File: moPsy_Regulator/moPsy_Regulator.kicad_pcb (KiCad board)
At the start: 2 copper layers, 96.5 x 50.8 mm, 23 parts, among them J1 Conn_01x01_Pin, J2 Conn_01x01_Pin, J3 Conn_01x01_Pin, J4 Conn_01x01_Pin, Q1 BD201, Q2 BC337, U1 LM723_DIP14

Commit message: Small fixes and Greographic Renumeration
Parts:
- renumbered C4 to C1, C1 to C4, J4 to J3, J3 to J4
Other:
- board text removed: "0R"
- board text removed: "DNP"
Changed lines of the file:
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@@
 		(descr "C, Disc series, Radial, pin pitch=5.00mm, , diameter*width=4.3*1.9mm^2, Capacitor, http://www.vishay.com/docs/45233/krseries.pdf")
 		(tags "C Disc series Radial pin pitch 5.00mm  diameter 4.3mm width 1.9mm Capacitor")
-		(property "Reference" "C4"
+		(property "Reference" "C1"
 			(at 2.54 -0.204999 360)
 			(layer "F.SilkS")
@@
 		(layer "F.Cu")
 		(at 191.77 96.52)
-		(property "Reference" "J3"
+		(property "Reference" "J4"
 			(at 7 0 360)
 			(layer "F.SilkS")
@@
 		(layer "F.Cu")
 		(at 177.84 96.52)
-		(property "Reference" "J4"
+		(property "Reference" "J3"
 			(at 7 0 360)
 			(layer "F.SilkS")
@@
 		(descr "CP, Radial series, Radial, pin pitch=7.50mm, , diameter=16mm, Electrolytic Capacitor")
 		(tags "CP Radial series Radial pin pitch 7.50mm  diameter 16mm Electrolytic Capacitor")
-		(property "Reference" "C1"
+		(property "Reference" "C4"
 			(at 1.27 -3.81 180)
 			(layer "F.SilkS")
@@
 		)
 	)
+	(gr_circle
+		(center 136.144 91.567)
+		(end 136.271 91.567)
+		(stroke
+			(width 0.1)
+			(type solid)
+		)
+		(fill solid)
+		(layer "F.SilkS")
+	)
+	(gr_line
+		(start 145.161 90.297)
+		(end 147.701 90.297)
+		(stroke
+			(width 0.1)
+			(type default)
+		)
+		(layer "F.SilkS")
+	)
+	(gr_circle
+		(center 145.161 90.297)
+		(end 145.288 90.297)
+		(stroke
+			(width 0.1)
+			(type solid)
+		)
+		(fill solid)
+		(layer "F.SilkS")
+	)
+	(gr_circle
+		(center 147.701 90.297)
+		(end 147.828 90.297)
+		(stroke
+			(width 0.1)
+			(type solid)
+		)
+		(fill solid)
+		(layer "F.SilkS")
+	)
 	(gr_line
 		(start 132.715 89.408)
@@
 	)
 	(gr_line
+		(start 133.604 91.567)
+		(end 136.144 91.567)
+		(stroke
+			(width 0.1)
+			(type default)
+		)
+		(layer "F.SilkS")
+	)
+	(gr_circle
+		(center 133.604 91.567)
+		(end 133.731 91.567)
+		(stroke
+			(width 0.1)
+			(type solid)
+		)
+		(fill solid)
+		(layer "F.SilkS")
+	)
+	(gr_line
 		(start 132.715 89.408)
 		(end 131.191 87.884)
@@
 	)
 	(gr_line
+		(start 138.938 91.821)
+		(end 139.446 91.186)
+		(stroke
+			(width 0.1)
+			(type default)
+		)
+		(layer "F.SilkS")
+	)
+	(gr_line
 		(start 132.715 91.948)
 		(end 132.715 89.408)
@@
 	)
 	(gr_line
+		(start 138.938 91.186)
+		(end 139.446 91.821)
+		(stroke
+			(width 0.1)
+			(type default)
+		)
+		(layer "F.SilkS")
+	)
+	(gr_line
+		(start 150.368 89.9795)
+		(end 150.876 90.6145)
+		(stroke
+			(width 0.1)
+			(type default)
+		)
+		(layer "F.SilkS")
+	)
+	(gr_line
 		(start 114.7445 94.742)
 		(end 113.0935 88.265)
@@
 		(layer "F.SilkS")
 	)
+	(gr_line
+		(start 150.368 90.6145)
+		(end 150.876 89.9795)
+		(stroke
+			(width 0.1)
+			(type default)
+		)
+		(layer "F.SilkS")
+	)
 	(gr_rect
 		(start 101.6 50.8)
@@
 		)
 	)
-	(gr_text "0R"
-		(at 136.525 92.075 0)
-		(layer "F.SilkS")
-		(effects
-			(font
-				(size 0.8 0.8)
-				(thickness 0.1)
-			)
-			(justify right bottom)
-		)
-	)
 	(gr_text "500R"
 		(at 136.525 90.805 0)
@@
 		)
 	)
-	(gr_text "DNP"
-		(at 140.335 92.075 0)
-		(layer "F.SilkS")
-		(effects
-			(font
-				(size 0.8 0.8)
-				(thickness 0.1)
-			)
-			(justify right bottom)
-		)
-	)
 	(gr_text "V_{OUT}"
 		(at 191.77 100.838 0)
@@
 		)
 	)
-	(gr_text "DNP"
-		(at 151.765 90.805 0)
-		(layer "F.SilkS")
-		(effects
-			(font
-				(size 0.8 0.8)
-				(thickness 0.1)
-			)
-			(justify right bottom)
-		)
-	)
 	(gr_text "1k"
 		(at 147.955 92.075 0)
@@
 		)
 	)
-	(gr_text "0R"
-		(at 147.955 90.805 0)
-		(layer "F.SilkS")
-		(effects
-			(font
-				(size 0.8 0.8)
-				(thickness 0.1)
-			)
-			(justify right bottom)
-		)
-	)
 	(segment
 		(start 141.605 68.58)
@@
 		)
 	)
+	(group ""
+		(members "07f13dc1-afab-4ed4-8025-a04d3f19f5e8" "46d33b63-7861-44c6-9e5e-61609bf35534"
+			"4a4c9e23-7bda-48f4-84c6-1a3d4b97ff38"
+		)
+	)
+	(group ""
+		(members "099868f8-a03c-43de-a861-8a08c08919b7" "15b0ae34-e2e2-4f86-aa7e-9aa4b8101d5a"
+			"16f80a3a-df75-4565-bd00-cf7e78347348"
+		)
+	)
+	(group ""
+		(members "94caba43-0bac-4706-8947-572840e6577d" "d404e082-68a9-48c7-a333-d59657457921")
+	)
+	(group ""
+		(members "de9c32ee-4f5a-437d-88a5-43bda4c5d7c3" "e727caf5-7b4a-46a1-b502-8a09c3ae42dc")
+	)
 )

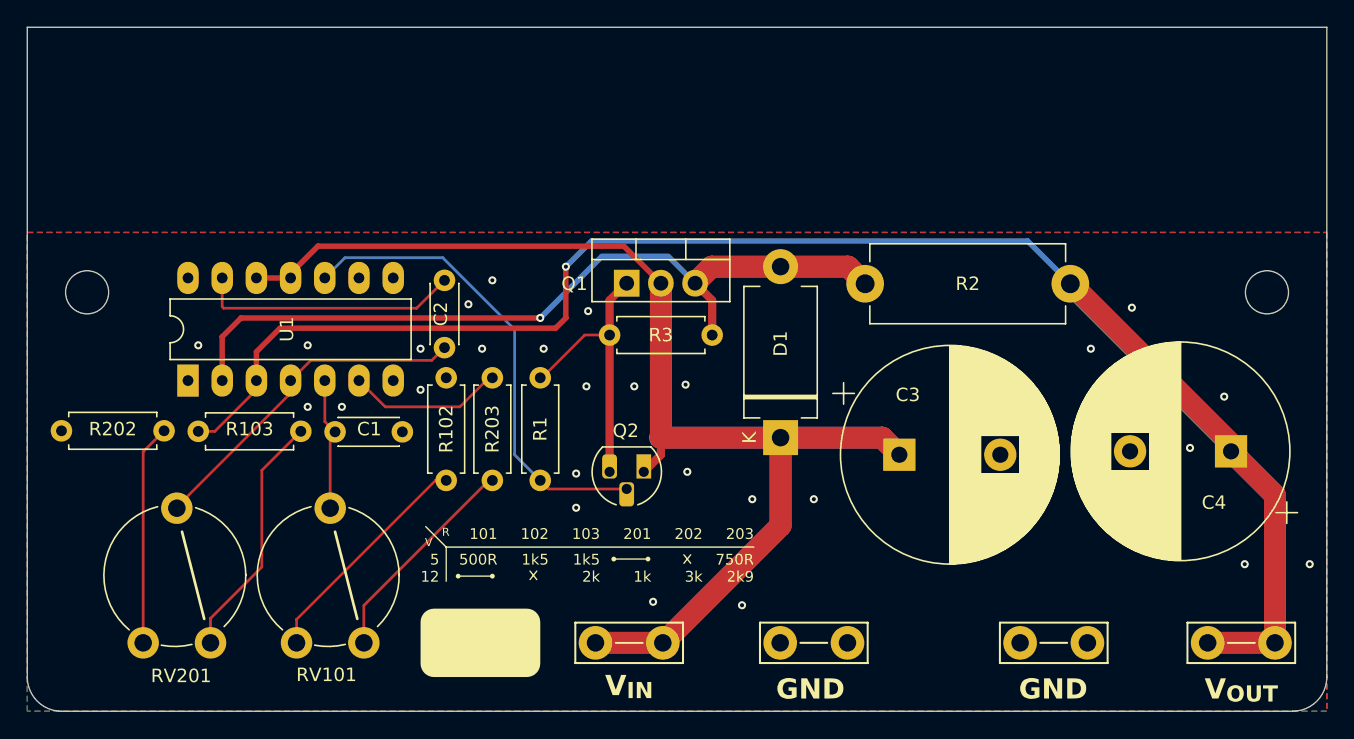
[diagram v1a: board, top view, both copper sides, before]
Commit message: Improve the voltage selection and layout
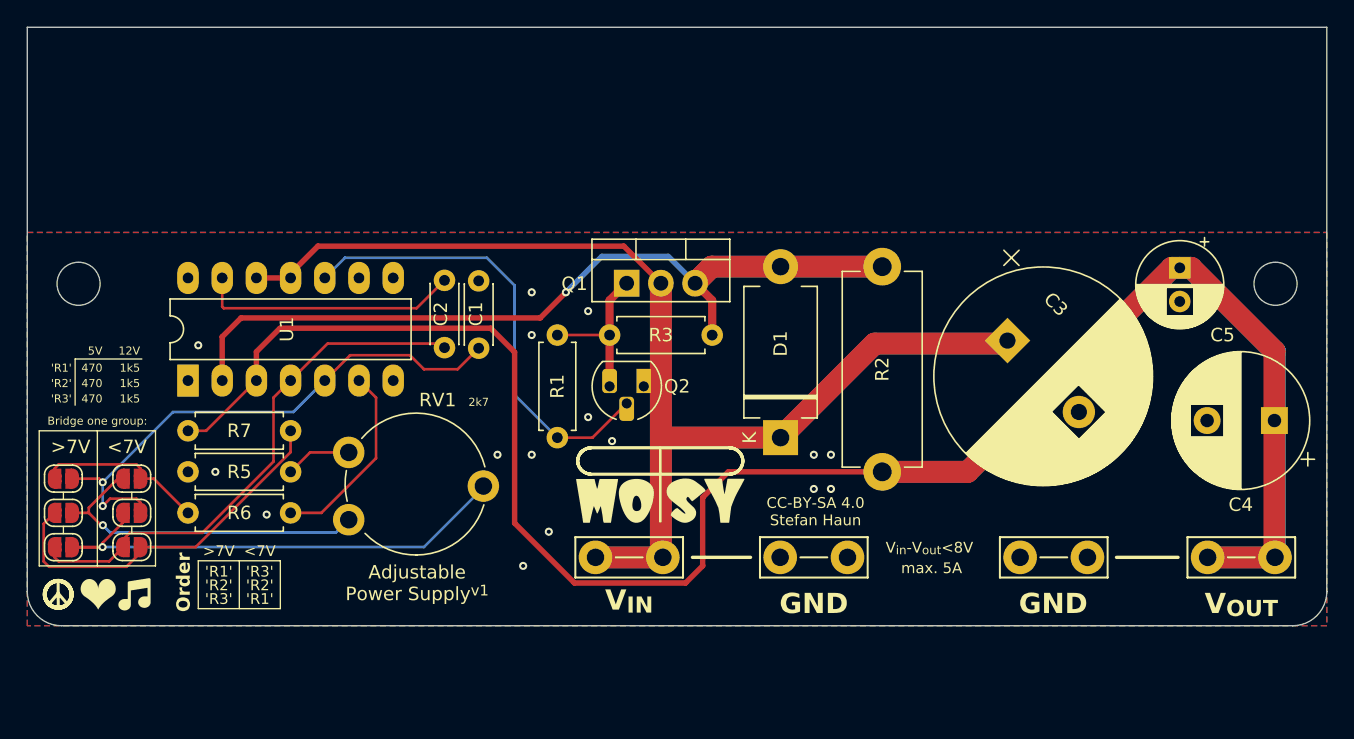
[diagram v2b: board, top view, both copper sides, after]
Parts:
- removed R102, R202: "R2", Resistor_THT:R_Axial_DIN0207_L6.3mm_D2.5mm_P7.62mm_Horizontal
- removed R103, R203: "R3", Resistor_THT:R_Axial_DIN0207_L6.3mm_D2.5mm_P7.62mm_Horizontal
- removed REF** (x2): MountingHole_3.2mm_M3, MountingHole:MountingHole_3.2mm_M3
- removed RV101, RV201: "R1", Potentiometer_THT:Potentiometer_Piher_PT-10-V10_Vertical
- added C5: 22u, Capacitor_THT:CP_Radial_D6.3mm_P2.50mm, F.Cu at (187.2, 68.7)
- added JP11: SolderJumper_2_Open, Jumper:SolderJumper-2_P1.3mm_Open_RoundedPad1.0x1.5mm, F.Cu at (109.4, 84.3)
- added JP12: SolderJumper_2_Open, Jumper:SolderJumper-2_P1.3mm_Open_RoundedPad1.0x1.5mm, F.Cu at (109.4, 86.9)
- added JP13: SolderJumper_2_Open, Jumper:SolderJumper-2_P1.3mm_Open_RoundedPad1.0x1.5mm, F.Cu at (109.4, 89.4)
- added JP21: SolderJumper_2_Open, Jumper:SolderJumper-2_P1.3mm_Open_RoundedPad1.0x1.5mm, F.Cu at (104.3, 86.9)
- added JP22: SolderJumper_2_Open, Jumper:SolderJumper-2_P1.3mm_Open_RoundedPad1.0x1.5mm, F.Cu at (104.3, 89.4)
- added JP23: SolderJumper_2_Open, Jumper:SolderJumper-2_P1.3mm_Open_RoundedPad1.0x1.5mm, F.Cu at (104.3, 84.3)
- added R5: "R2", Resistor_THT:R_Axial_DIN0207_L6.3mm_D2.5mm_P7.62mm_Horizontal, F.Cu at (121.2, 83.8)
- added R6: "R1"/"R3", Resistor_THT:R_Axial_DIN0207_L6.3mm_D2.5mm_P7.62mm_Horizontal, F.Cu at (121.2, 86.9)
- added R7: "R1"/"R3", Resistor_THT:R_Axial_DIN0207_L6.3mm_D2.5mm_P7.62mm_Horizontal, F.Cu at (113.5, 80.8)
- added REF1: MountingHole_3.2mm_M3, MountingHole:MountingHole_3.2mm_M3, F.Cu at (194.3, 69.8)
- added REF2: MountingHole_3.2mm_M3, MountingHole:MountingHole_3.2mm_M3, F.Cu at (105.4, 69.8)
- added RV1: "P1", Potentiometer_THT:Potentiometer_Piher_PT-10-V10_Vertical, F.Cu at (125.5, 87.4)
- C4: value 2200u -> 220u; footprint Capacitor_THT:CP_Radial_D16.0mm_P7.50mm -> Capacitor_THT:CP_Radial_D10.0mm_P5.00mm
- moved C1 12.3 mm to (135.1, 74.6), turned to 90 degrees
- moved C3 11.7 mm to (174.4, 74.1), turned to -45 degrees
- moved J1 6.35 mm to (146.3, 90.2)
- moved J2 6.35 mm to (160.0, 90.2)
- moved J3 6.35 mm to (177.8, 90.2)
- moved J4 6.35 mm to (191.8, 90.2)
- moved Q2 6.35 mm to (147.4, 77.5)
- moved C4 3.95 mm to (194.2, 80.0)
- moved R1 3.42 mm to (141.0, 81.3)
- moved R2 1.80 mm to (165.1, 68.6), turned to -90 degrees
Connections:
- net Net-(U1-+) renamed LV_{center}
- net Net-(U1--) renamed HV_{center}
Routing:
- net V_{out}: track 151.8 -> 194.9 mm, vias 1 -> 0
- net Net-(JP12-B): track 0.00 -> 37.9 mm, vias 0 -> 1
- net LV_{center}: track 9.94 -> 41.0 mm, vias 0 -> 2
- net HV_{top}: track 0.00 -> 28.5 mm
- net Net-(JP11-B): track 0.00 -> 25.4 mm, vias 0 -> 1
- net Net-(R103-Pad2): track 18.5 -> 0.00 mm
- net Net-(R102-Pad1): track 17.1 -> 0.00 mm
- net Net-(R202-Pad1): track 16.4 -> 0.00 mm
- net Net-(R203-Pad2): track 16.2 -> 0.00 mm
- net HV_{center}: track 25.4 -> 40.7 mm
- net LV_{top}: track 0.00 -> 13.3 mm
- net Net-(Q1-B): track 21.0 -> 12.1 mm
- net Net-(R5-Pad1): track 0.00 -> 4.92 mm
- net Net-(U1-VREF): track 11.6 -> 14.3 mm
- net Net-(D1-A): track 73.4 -> 74.9 mm
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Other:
- board size 96.5 x 50.8 mm -> 96.5 x 44.5 mm
- board text added: "'R1'"
- board text added: "'R2'"
- board text added: "'R3'"
- board text added: "12V"
- board text added: "2k7"
- board text added: "470"
- board text added: "5V"
- board text added: "<7V"
- board text added: ">7V"
- board text added: "Adjustable Power Supply^{v1}"
- board text added: "Bridge one group:"
- board text added: "CC-BY-SA 4.0 Stefan Haun"
- board text added: "Order"
- board text added: "V_{in}-V_{out}<8V"
- board text added: "max. 5A"
- board text removed: "101"
- board text removed: "102"
- board text removed: "103"
- board text removed: "12"
- board text removed: "1k"
- board text removed: "201"
- board text removed: "202"
- board text removed: "203"
- board text removed: "2k"
- board text removed: "2k9"
- board text removed: "3k"
- board text removed: "5"
- board text removed: "500R"
- board text removed: "750R"
- board text removed: "R"
- board text removed: "V"

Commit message: Geographical Reannotation and some minor fixes
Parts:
- renumbered C2 to C1, C1 to C2, C5 to C4, C4 to C5, JP23 to JP1, JP21 to JP2, JP22 to JP3, JP11 to JP4, JP12 to JP5, JP13 to JP6, R7 to R1, R5 to R2, R6 to R3, R1 to R4, R3 to R5, R2 to R6, REF2 to REF1, REF1 to REF2
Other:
- board text added: "R1"
- board text added: "R1/R3"
- board text added: "R2"
- board text added: "R3"
- board text added: "R3/R1"
- board text removed: "'R1'"
- board text removed: "'R2'"
- board text removed: "'R3'"
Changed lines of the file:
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@@
 		(descr "CP, Radial series, Radial, pin pitch=2.50mm, , diameter=6.3mm, Electrolytic Capacitor")
 		(tags "CP Radial series Radial pin pitch 2.50mm  diameter 6.3mm Electrolytic Capacitor")
-		(property "Reference" "C5"
+		(property "Reference" "C4"
 			(at 4.99238 -3.175 180)
 			(layer "F.SilkS")
@@
 		(descr "Resistor, Axial_DIN0207 series, Axial, Horizontal, pin pitch=7.62mm, 0.25W = 1/4W, length*diameter=6.3*2.5mm^2, http://cdn-reichelt.de/documents/datenblatt/B400/1_4W%23YAG.pdf")
 		(tags "Resistor Axial_DIN0207 series Axial Horizontal pin pitch 7.62mm 0.25W = 1/4W length 6.3mm diameter 2.5mm")
-		(property "Reference" "R7"
+		(property "Reference" "R1"
 			(at 3.81 0 0)
 			(layer "F.SilkS")
+			(hide yes)
 			(effects
 				(font
@@
 		(descr "SMD Solder Jumper, 1x1.5mm, rounded Pads, 0.3mm gap, open")
 		(tags "solder jumper open")
-		(property "Reference" "JP21"
+		(property "Reference" "JP2"
 			(at -3.175 0.018 360)
 			(layer "F.SilkS")
@@
 		(descr "Resistor, Axial_DIN0614 series, Axial, Horizontal, pin pitch=15.24mm, 1.5W, length*diameter=14.3*5.7mm^2")
 		(tags "Resistor Axial_DIN0614 series Axial Horizontal pin pitch 15.24mm 1.5W length 14.3mm diameter 5.7mm")
-		(property "Reference" "R2"
+		(property "Reference" "R6"
 			(at 7.62 0 90)
 			(layer "F.SilkS")
@@
 		(descr "C, Disc series, Radial, pin pitch=5.00mm, , diameter*width=4.3*1.9mm^2, Capacitor, http://www.vishay.com/docs/45233/krseries.pdf")
 		(tags "C Disc series Radial pin pitch 5.00mm  diameter 4.3mm width 1.9mm Capacitor")
-		(property "Reference" "C1"
+		(property "Reference" "C2"
 			(at 2.54 -0.204999 270)
 			(layer "F.SilkS")
@@
 		(descr "SMD Solder Jumper, 1x1.5mm, rounded Pads, 0.3mm gap, open")
 		(tags "solder jumper open")
-		(property "Reference" "JP12"
+		(property "Reference" "JP5"
 			(at -3.19 0.254 180)
 			(layer "F.SilkS")
@@
 		(descr "SMD Solder Jumper, 1x1.5mm, rounded Pads, 0.3mm gap, open")
 		(tags "solder jumper open")
-		(property "Reference" "JP22"
+		(property "Reference" "JP3"
 			(at -3.414 -0.006 360)
 			(layer "F.SilkS")
@@
 		(descr "C, Disc series, Radial, pin pitch=5.00mm, , diameter*width=4.3*1.9mm^2, Capacitor, http://www.vishay.com/docs/45233/krseries.pdf")
 		(tags "C Disc series Radial pin pitch 5.00mm  diameter 4.3mm width 1.9mm Capacitor")
-		(property "Reference" "C2"
+		(property "Reference" "C1"
 			(at 2.5 0.274999 90)
 			(layer "F.SilkS")
@@
 		(descr "Resistor, Axial_DIN0207 series, Axial, Horizontal, pin pitch=7.62mm, 0.25W = 1/4W, length*diameter=6.3*2.5mm^2, http://cdn-reichelt.de/documents/datenblatt/B400/1_4W%23YAG.pdf")
 		(tags "Resistor Axial_DIN0207 series Axial Horizontal pin pitch 7.62mm 0.25W = 1/4W length 6.3mm diameter 2.5mm")
-		(property "Reference" "R5"
+		(property "Reference" "R2"
 			(at 3.81 0 180)
 			(layer "F.SilkS")
@@
 		(descr "Mounting Hole 3.2mm, no annular, M3")
 		(tags "mounting hole 3.2mm no annular m3")
-		(property "Reference" "REF1"
+		(property "Reference" "REF2"
 			(at 0 -4.2 0)
 			(layer "F.SilkS")
@@
 		(descr "Resistor, Axial_DIN0207 series, Axial, Horizontal, pin pitch=7.62mm, 0.25W = 1/4W, length*diameter=6.3*2.5mm^2, http://cdn-reichelt.de/documents/datenblatt/B400/1_4W%23YAG.pdf")
 		(tags "Resistor Axial_DIN0207 series Axial Horizontal pin pitch 7.62mm 0.25W = 1/4W length 6.3mm diameter 2.5mm")
-		(property "Reference" "R1"
+		(property "Reference" "R4"
 			(at 3.81 0 -90)
 			(layer "F.SilkS")
@@
 		(descr "Resistor, Axial_DIN0207 series, Axial, Horizontal, pin pitch=7.62mm, 0.25W = 1/4W, length*diameter=6.3*2.5mm^2, http://cdn-reichelt.de/documents/datenblatt/B400/1_4W%23YAG.pdf")
 		(tags "Resistor Axial_DIN0207 series Axial Horizontal pin pitch 7.62mm 0.25W = 1/4W length 6.3mm diameter 2.5mm")
-		(property "Reference" "R6"
+		(property "Reference" "R3"
 			(at 3.81 0 180)
 			(layer "F.SilkS")
+			(hide yes)
 			(effects
 				(font
@@
 		(descr "SMD Solder Jumper, 1x1.5mm, rounded Pads, 0.3mm gap, open")
 		(tags "solder jumper open")
-		(property "Reference" "JP13"
+		(property "Reference" "JP6"
 			(at -3.351 0.26 180)
 			(layer "F.SilkS")
@@
 		(descr "CP, Radial series, Radial, pin pitch=5.00mm, , diameter=10mm, Electrolytic Capacitor")
 		(tags "CP Radial series Radial pin pitch 5.00mm  diameter 10mm Electrolytic Capacitor")
-		(property "Reference" "C4"
+		(property "Reference" "C5"
 			(at 2.5 -6.25 180)
 			(layer "F.SilkS")
@@
 		(descr "SMD Solder Jumper, 1x1.5mm, rounded Pads, 0.3mm gap, open")
 		(tags "solder jumper open")
-		(property "Reference" "JP23"
+		(property "Reference" "JP1"
 			(at -3.414 0 360)
 			(layer "F.SilkS")
@@
 		(descr "Resistor, Axial_DIN0207 series, Axial, Horizontal, pin pitch=7.62mm, 0.25W = 1/4W, length*diameter=6.3*2.5mm^2, http://cdn-reichelt.de/documents/datenblatt/B400/1_4W%23YAG.pdf")
 		(tags "Resistor Axial_DIN0207 series Axial Horizontal pin pitch 7.62mm 0.25W = 1/4W length 6.3mm diameter 2.5mm")
-		(property "Reference" "R3"
+		(property "Reference" "R5"
 			(at 3.81 0 0)
 			(layer "F.SilkS")
@@
 		(descr "Mounting Hole 3.2mm, no annular, M3")
 		(tags "mounting hole 3.2mm no annular m3")
-		(property "Reference" "REF2"
+		(property "Reference" "REF1"
 			(at 0 -4.2 0)
 			(layer "F.SilkS")
@@
 		(descr "SMD Solder Jumper, 1x1.5mm, rounded Pads, 0.3mm gap, open")
 		(tags "solder jumper open")
-		(property "Reference" "JP11"
+		(property "Reference" "JP4"
 			(at -3.19 0.248 180)
 			(layer "F.SilkS")
@@
 	)
 	(gr_line
-		(start 105.156 78.867)
-		(end 105.156 75.438)
+		(start 104.775 78.486)
+		(end 104.775 75.057)
 		(stroke
 			(width 0.1)
@@
 	)
 	(gr_line
-		(start 105.156 75.438)
-		(end 110.109 75.438)
+		(start 104.775 75.057)
+		(end 109.728 75.057)
 		(stroke
 			(width 0.1)
@@
 	)
 	(gr_text "1k5"
-		(at 109.982 78.74 0)
+		(at 109.601 78.359 0)
 		(layer "F.SilkS")
 		(effects
@@
 	)
 	(gr_text "470"
-		(at 107.188 78.74 0)
+		(at 106.807 78.359 0)
 		(layer "F.SilkS")
 		(effects
@@
 		)
 	)
-	(gr_text "'R3'"
-		(at 104.902 78.74 0)
+	(gr_text "R3"
+		(at 104.521 78.359 0)
 		(layer "F.SilkS")
 		(effects
@@
 	)
 	(gr_text "470"
-		(at 107.188 76.454 0)
+		(at 106.807 76.073 0)
 		(layer "F.SilkS")
 		(effects
@@
 		)
 	)
-	(gr_text "'R1'"
+	(gr_text "R1"
 		(at 118.872 93.726 0)
 		(layer "F.SilkS")
@@
 		)
 	)
-	(gr_text "'R3'"
+	(gr_text "R3"
 		(at 118.872 91.694 0)
 		(layer "F.SilkS")
@@
 	)
 	(gr_text "1k5"
-		(at 109.982 76.454 0)
+		(at 109.601 76.073 0)
 		(layer "F.SilkS")
 		(effects
@@
 		)
 	)
-	(gr_text "'R2'"
-		(at 104.902 77.597 0)
+	(gr_text "R2"
+		(at 104.521 77.216 0)
 		(layer "F.SilkS")
 		(effects
@@
 		)
 	)
-	(gr_text "'R2'"
+	(gr_text "R2"
 		(at 115.824 92.71 0)
 		(layer "F.SilkS")
@@
 		)
 	)
-	(gr_text "'R2'"
+	(gr_text "R2"
 		(at 118.872 92.71 0)
 		(layer "F.SilkS")
@@
 		)
 	)
-	(gr_text "'R1'"
-		(at 104.902 76.454 0)
+	(gr_text "R1"
+		(at 104.521 76.073 0)
 		(layer "F.SilkS")
 		(effects
@@
 		)
 	)
+	(gr_text "R3/R1"
+		(at 117.094 87.503 0)
+		(layer "F.SilkS")
+		(effects
+			(font
+				(size 1 1)
+				(thickness 0.15)
+			)
+			(justify bottom)
+		)
+	)
 	(gr_text ">7V"
 		(at 115.824 90.17 0)
@@
 	)
 	(gr_text "5V"
-		(at 107.188 75.184 0)
+		(at 106.807 74.803 0)
 		(layer "F.SilkS")
 		(effects
@@
 	)
 	(gr_text "12V"
-		(at 109.982 75.184 0)
+		(at 109.601 74.803 0)
 		(layer "F.SilkS")
 		(effects
@@
 	)
 	(gr_text "470"
-		(at 107.188 77.597 0)
+		(at 106.807 77.216 0)
 		(layer "F.SilkS")
 		(effects
@@
 		)
 	)
-	(gr_text "'R3'"
+	(gr_text "R3"
 		(at 115.824 93.726 0)
 		(layer "F.SilkS")
@@
 		)
 	)
-	(gr_text "'R1'"
+	(gr_text "R1/R3"
+		(at 117.221 81.407 0)
+		(layer "F.SilkS")
+		(effects
+			(font
+				(size 1 1)
+				(thickness 0.15)
+			)
+			(justify bottom)
+		)
+	)
+	(gr_text "R1"
 		(at 115.824 91.694 0)
 		(layer "F.SilkS")
@@
 	)
 	(gr_text "1k5"
-		(at 109.982 77.597 0)
+		(at 109.601 77.216 0)
 		(layer "F.SilkS")
 		(effects
@@
 	)
 	(via
-		(at 138.43 90.805)
+		(at 138.43 90.17)
 		(size 0.6)
 		(drill 0.3)
@@
 	)
 	(via
-		(at 119.38 86.995)
+		(at 119.634 85.979)
 		(size 0.6)
 		(drill 0.3)
@@
 	)
 	(segment
+		(start 139.7 72.39)
+		(end 117.475 72.39)
+		(width 0.4064)
+		(layer "F.Cu")
+		(net 7)
+	)
+	(segment
 		(start 152.43 68.58)
 		(end 151.2 69.81)
@@
 	)
 	(segment
+		(start 117.475 72.39)
+		(end 116.078 73.787)
+		(width 0.4064)
+		(layer "F.Cu")
+		(net 7)
+	)
+	(segment
 		(start 157.55 68.58)
 		(end 165.099998 68.58)
@@
 	)
 	(segment
-		(start 139.7 72.39)
-		(end 117.475 72.39)
+		(start 141.1605 70.9295)
+		(end 139.7 72.39)
 		(width 0.4064)
 		(layer "F.Cu")
@@
 	)
 	(segment
-		(start 117.475 72.39)
-		(end 116.078 73.787)
-		(width 0.4064)
-		(layer "F.Cu")
-		(net 7)
-	)
-	(segment
 		(start 116.078 73.787)
 		(end 116.078 77.039999)
@@
 		(net 7)
 	)
-	(segment
-		(start 141.605 70.485)
-		(end 139.7 72.39)
-		(width 0.4064)
-		(layer "F.Cu")
-		(net 7)
-	)
 	(via
-		(at 141.605 70.485)
+		(at 141.1605 70.9295)
 		(size 0.6)
 		(drill 0.3)
@@
 	)
 	(segment
-		(start 144.272 67.818)
-		(end 149.208 67.818)
-		(width 0.4064)
-		(layer "B.Cu")
-		(net 7)
-	)
-	(segment
-		(start 141.605 70.485)
+		(start 141.1605 70.9295)
 		(end 144.272 67.818)
 		(width 0.4064)
@@
 		(layer "B.Cu")
 		(net 7)
+	)
+	(segment
+		(start 144.272 67.818)
+		(end 149.208 67.818)
+		(width 0.4064)
+		(layer "B.Cu")
+		(net 7)
